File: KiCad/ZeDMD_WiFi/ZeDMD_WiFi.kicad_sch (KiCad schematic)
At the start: 18 parts, among them J1 max98357-L, J10 Conn_01x02_Pin, J11 Conn_01x02_Pin, J2 MicroSD, J3 max98357-R, J4 MAX_Vin_SELECT, J5 RGBout_SELECT, J6 5Vin_OPTION, J7 KF7.62 Barrier Terminal Block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, J8 USB-C breakout

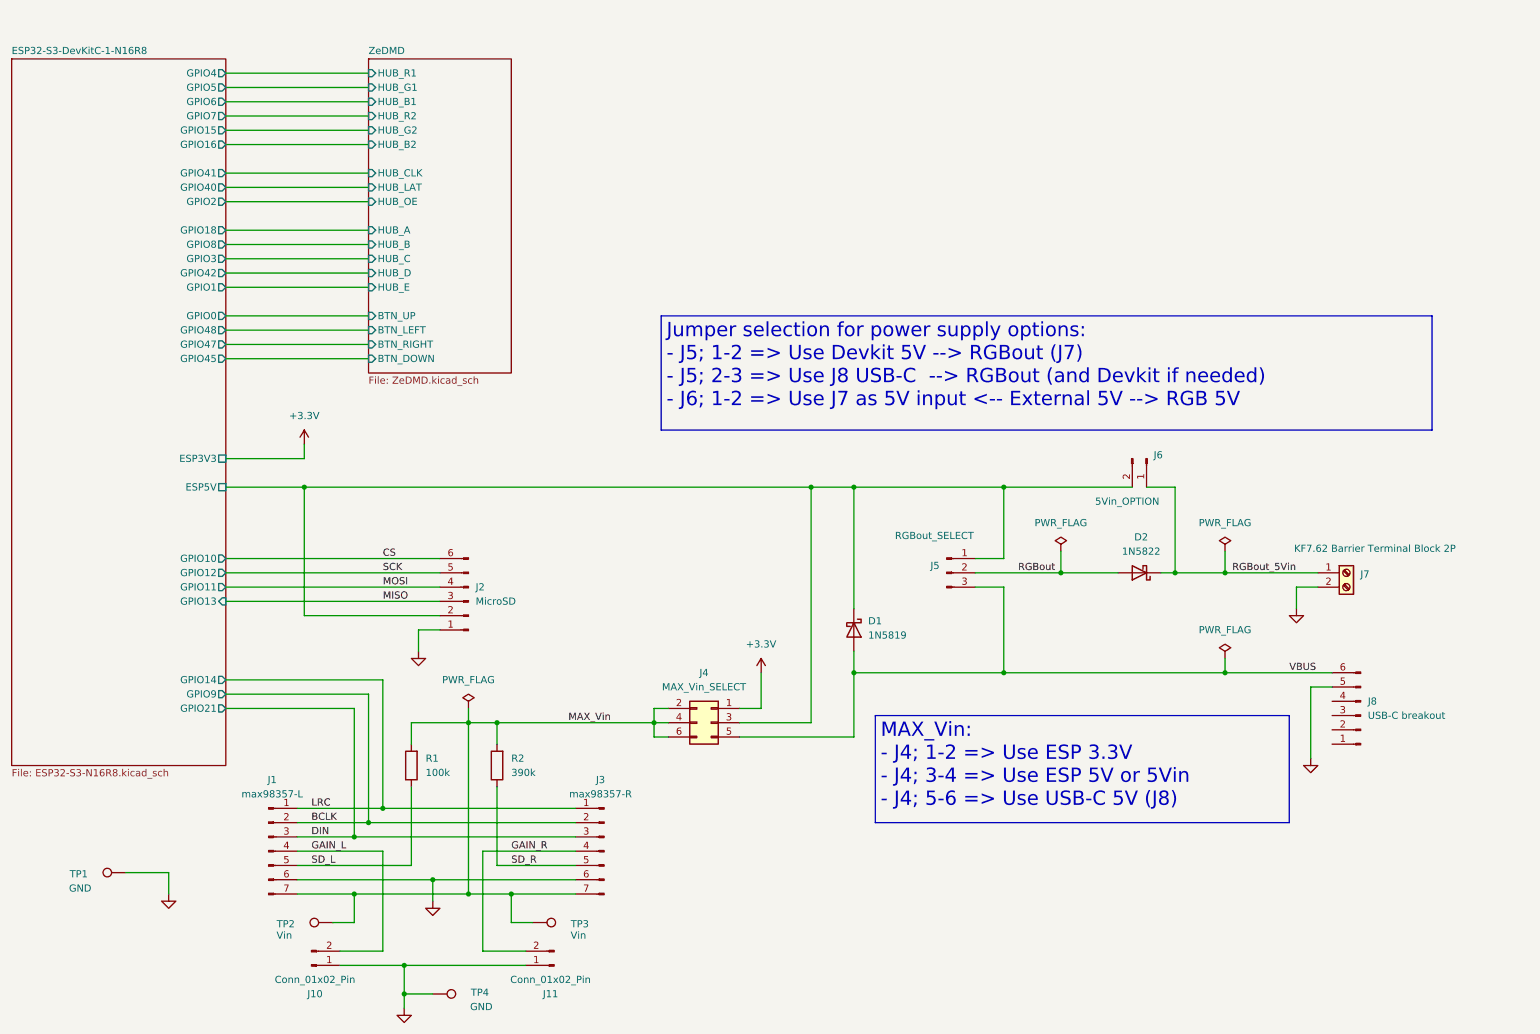
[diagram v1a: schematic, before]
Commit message: Update PCB to Rev1.3
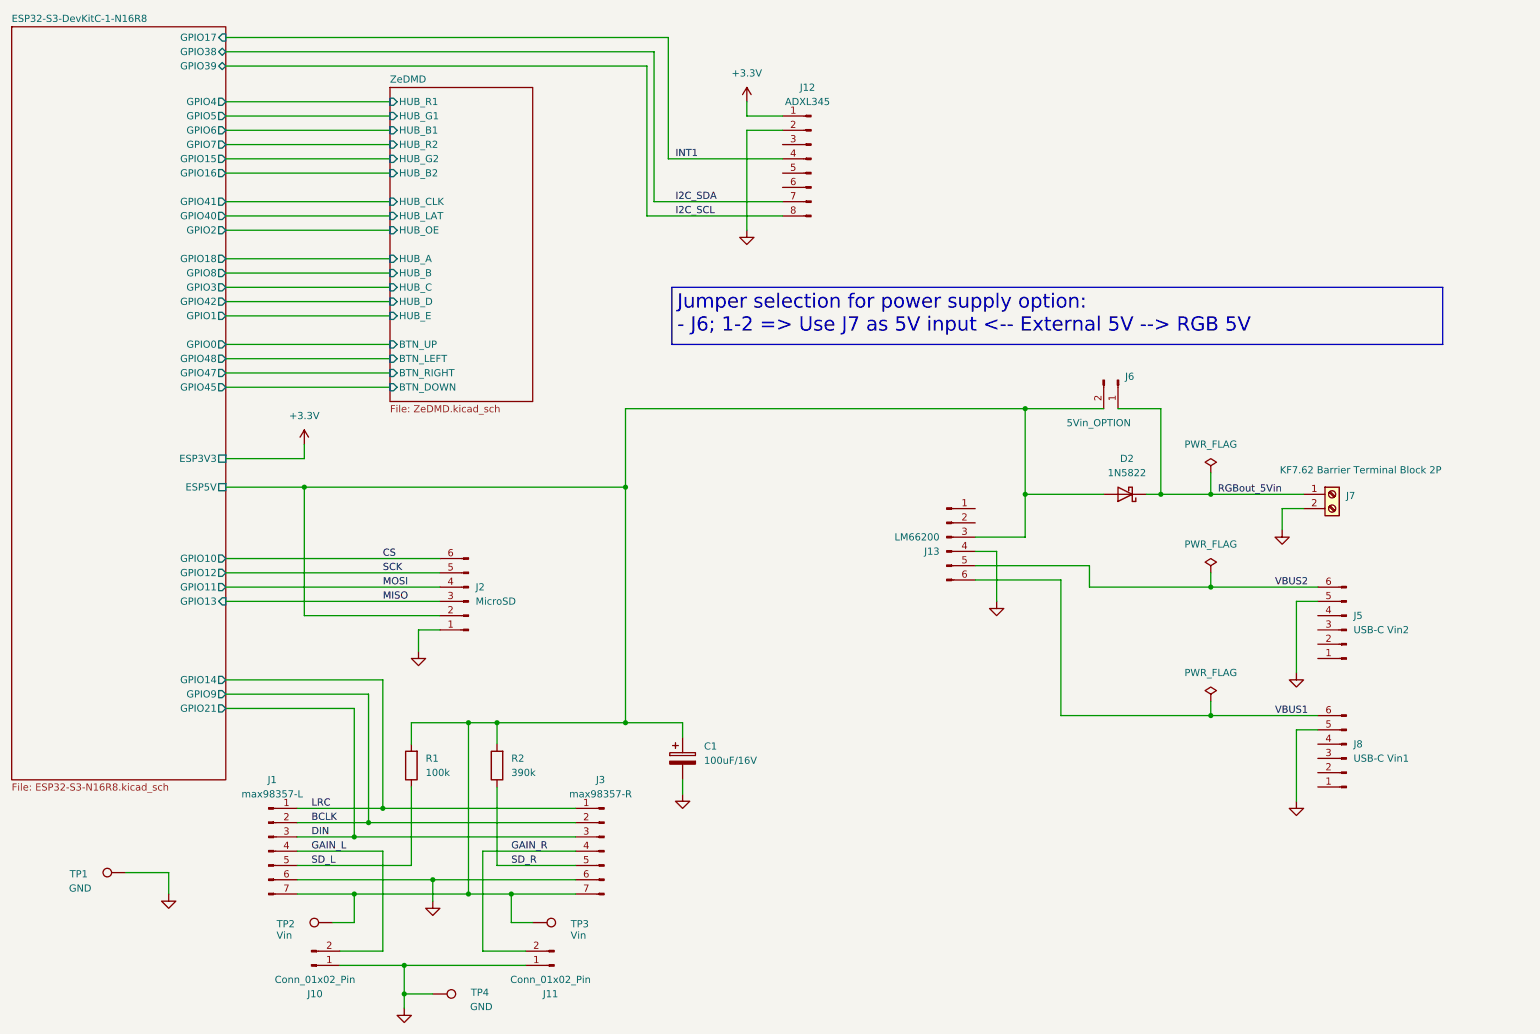
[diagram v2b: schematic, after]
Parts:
- removed D1: 1N5819, Diode_THT:D_DO-41_SOD81_P10.16mm_Horizontal, symbol Diode:1N5819
- removed J4: MAX_Vin_SELECT, Connector_PinHeader_2.54mm:PinHeader_2x03_P2.54mm_Vertical, symbol Connector_Generic:Conn_02x03_Odd_Even
- removed J5: RGBout_SELECT, Connector_PinHeader_2.54mm:PinHeader_1x03_P2.54mm_Vertical, symbol Connector:Conn_01x03_Pin
- added C1: 100uF/16V, Capacitor_THT:CP_Radial_D8.0mm_P2.50mm, symbol Device:C_Polarized
- added J12: ADXL345, Connector_PinHeader_2.54mm:PinHeader_1x08_P2.54mm_Vertical, symbol Connector:Conn_01x08_Pin
- added J13: LM66200, Connector_PinSocket_2.54mm:PinSocket_1x06_P2.54mm_Vertical, symbol Connector:Conn_01x06_Pin
- added J5: USB-C Vin2, Connector_PinSocket_2.54mm:PinSocket_1x06_P2.54mm_Vertical, symbol Connector:Conn_01x06_Pin
- J8: value USB-C breakout -> USB-C Vin1
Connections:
- net MAX_Vin is gone; now on net ESP32-S3-DevKitC-1-N16R8/ESP5V: J1.7 (Pin_7), J3.7 (Pin_7), R1.2, R2.2, TP2.1, TP3.1
- net RGBout is gone; now on net ESP32-S3-DevKitC-1-N16R8/ESP5V: D2.2 (A)
- net +3.3V: now also J12.1 (Pin_1)
- net ESP32-S3-DevKitC-1-N16R8/ESP5V: now also C1.1, J13.3 (Pin_3)
- net GND: now also C1.2, J12.2 (Pin_2), J13.4 (Pin_4), J5.5 (Pin_5)
- net VBUS renamed VBUS1
- net VBUS1: now also J13.6 (Pin_6)
- new net I2C_SCL: J12.8 (Pin_8)
- new net I2C_SDA: J12.7 (Pin_7)
- new net INT1: J12.4 (Pin_4)
- new net VBUS2: J13.5 (Pin_5), J5.6 (Pin_6)
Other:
- sheet ESP32-S3-DevKitC-1-N16R8 ports: added GPIO17, GPIO38, GPIO39; removed none
- moved on the sheet: D2, J6, J7, J8

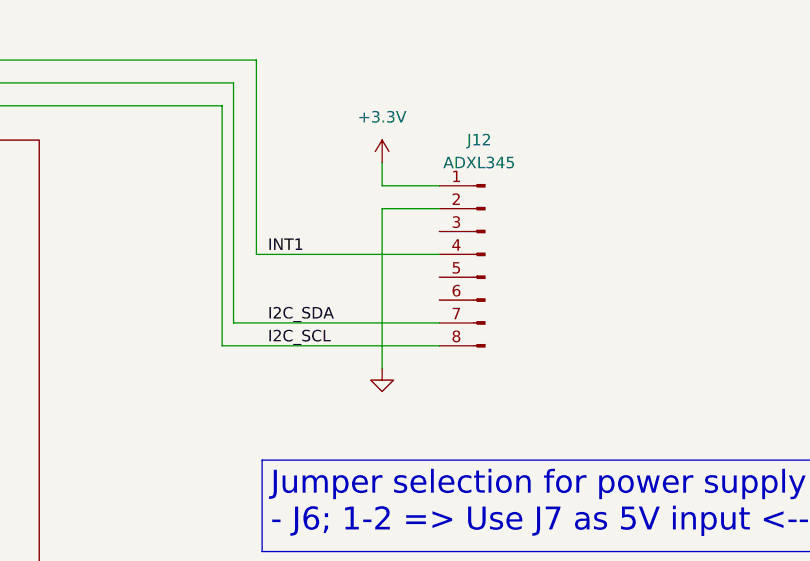
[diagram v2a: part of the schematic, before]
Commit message: Fix J12 reversed power supply pins
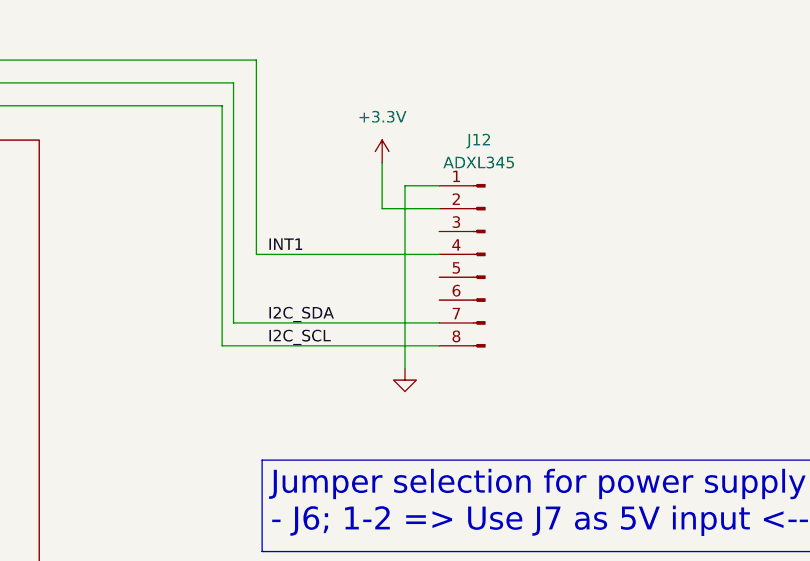
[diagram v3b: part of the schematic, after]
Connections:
- net +3.3V: now also J12.2 (Pin_2); no longer J12.1 (Pin_1)
- net GND: now also J12.1 (Pin_1); no longer J12.2 (Pin_2)
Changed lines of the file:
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@@
 	(title_block
 		(title "ZeDMD-WIFI-128x32")
-		(date "2026-09-04")
-		(rev "1.3")
+		(date "2026-09-19")
+		(rev "1.4")
 		(company "elabree")
 		(comment 1 "https://github.com/jens-b/The-Arcade")
@@
 	(wire
 		(pts
-			(xy 156.21 38.1) (xy 156.21 55.88)
+			(xy 229.87 102.87) (xy 238.76 102.87)
 		)
 		(stroke
@@
 	(wire
 		(pts
-			(xy 229.87 102.87) (xy 238.76 102.87)
+			(xy 144.78 143.51) (xy 144.78 146.05)
 		)
 		(stroke
@@
 	(wire
 		(pts
-			(xy 144.78 143.51) (xy 144.78 146.05)
+			(xy 158.75 35.56) (xy 158.75 55.88)
 		)
 		(stroke
@@
 	(wire
 		(pts
-			(xy 63.5 121.92) (xy 101.6 121.92)
+			(xy 158.75 35.56) (xy 162.56 35.56)
 		)
 		(stroke
@@
 	(wire
 		(pts
-			(xy 96.52 147.32) (xy 96.52 143.51)
+			(xy 63.5 121.92) (xy 101.6 121.92)
 		)
 		(stroke
@@
 	(wire
 		(pts
-			(xy 156.21 33.02) (xy 156.21 35.56)
+			(xy 96.52 147.32) (xy 96.52 143.51)
 		)
 		(stroke
@@
 	(wire
 		(pts
-			(xy 156.21 35.56) (xy 162.56 35.56)
+			(xy 156.21 38.1) (xy 162.56 38.1)
 		)
 		(stroke
@@
 	(wire
 		(pts
-			(xy 162.56 38.1) (xy 156.21 38.1)
-		)
-		(stroke
-			(width 0)
-			(type default)
-		)
-	)
-	(wire
-		(pts
 			(xy 106.68 143.51) (xy 111.76 143.51)
 		)
@@
 	(wire
 		(pts
+			(xy 156.21 33.02) (xy 156.21 38.1)
+		)
+		(stroke
+			(width 0)
+			(type default)
+		)
+	)
+	(wire
+		(pts
 			(xy 63.5 35.56) (xy 92.71 35.56)
 		)
@@
 	(symbol
 		(lib_id "power:GND")
-		(at 156.21 55.88 0)
+		(at 158.75 55.88 0)
 		(unit 1)
 		(body_style 1)
@@
 		(fields_autoplaced yes)
 		(property "Reference" "#PWR013"
-			(at 156.21 62.23 0)
+			(at 158.75 62.23 0)
 			(hide yes)
 			(show_name no)
@@
 		)
 		(property "Value" "GND"
-			(at 156.21 60.96 0)
+			(at 158.75 60.96 0)
 			(hide yes)
 			(show_name no)
@@
 		)
 		(property "Footprint" ""
-			(at 156.21 55.88 0)
+			(at 158.75 55.88 0)
 			(hide yes)
 			(show_name no)
@@
 		)
 		(property "Datasheet" ""
-			(at 156.21 55.88 0)
+			(at 158.75 55.88 0)
 			(hide yes)
 			(show_name no)
@@
 		)
 		(property "Description" "Power symbol creates a global label with name \"GND\" , ground"
-			(at 156.21 55.88 0)
+			(at 158.75 55.88 0)
 			(hide yes)
 			(show_name no)
